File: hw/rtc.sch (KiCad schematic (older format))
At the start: 0 parts

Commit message: hw: add RTC sheet
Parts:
- added BT?: Battery_Cell, symbol Battery_Cell
- added C?: 0.1, symbol C
- added DD?: DS3231, Housings_SOIC:SOIC-16W_7.5x10.3mm_Pitch1.27mm, symbol DS3231
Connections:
- net labels added: +3.3VP, GND, RPI_SCL, RPI_SDA, ~HAT_RST
- wire segments 0 -> 12
- no-connect marks 0 -> 2
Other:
- note added: "NOTE: That chip has integrated reset controller and 50k pull-up R."
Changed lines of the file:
@@
 Comment4 ""
 $EndDescr
+$Comp
+L DS3231 DD?
+U 1 1 5AB3B4DF
+P 4400 5000
+F 0 "DD?" H 4000 5450 60  0000 C CNN
+F 1 "DS3231" H 4400 4550 60  0000 C CNN
+F 2 "Housings_SOIC:SOIC-16W_7.5x10.3mm_Pitch1.27mm" H 4400 5050 60  0001 C CNN
+F 3 "" H 4400 5050 60  0001 C CNN
+	1    4400 5000
+	1    0    0    -1
+$EndComp
+$Comp
+L GND #PWR?
+U 1 1 5AB3BD10
+P 5350 5650
+F 0 "#PWR?" H 5350 5400 50  0001 C CNN
+F 1 "GND" H 5350 5500 50  0000 C CNN
+F 2 "" H 5350 5650 50  0001 C CNN
+F 3 "" H 5350 5650 50  0001 C CNN
+	1    5350 5650
+	1    0    0    -1
+$EndComp
+$Comp
+L +3.3VP #PWR?
+U 1 1 5AB3BD26
+P 5350 5100
+F 0 "#PWR?" H 5500 5050 50  0001 C CNN
+F 1 "+3.3VP" H 5350 5200 50  0000 C CNN
+F 2 "" H 5350 5100 50  0001 C CNN
+F 3 "" H 5350 5100 50  0001 C CNN
+	1    5350 5100
+	1    0    0    -1
+$EndComp
+Text GLabel 3200 4750 0    60   Output ~ 0
+~HAT_RST
+Wire Wire Line
+	3200 4750 3700 4750
+Text GLabel 3200 5250 0    60   Input ~ 0
+RPI_SCL
+Text GLabel 3200 5150 0    60   BiDi ~ 0
+RPI_SDA
+Wire Wire Line
+	3200 5150 3700 5150
+Wire Wire Line
+	3700 5250 3200 5250
+NoConn ~ 3700 5050
+NoConn ~ 5100 4750
+$Comp
+L C C?
+U 1 1 5AB3BFC6
+P 5350 5400
+F 0 "C?" H 5375 5500 50  0000 L CNN
+F 1 "0.1" H 5375 5300 50  0000 L CNN
+F 2 "" H 5388 5250 50  0001 C CNN
+F 3 "" H 5350 5400 50  0001 C CNN
+	1    5350 5400
+	1    0    0    -1
+$EndComp
+Wire Wire Line
+	5350 5100 5350 5250
+Wire Wire Line
+	5350 5550 5350 5650
+Wire Wire Line
+	5100 5250 5200 5250
+Wire Wire Line
+	5200 5250 5200 5600
+Wire Wire Line
+	5200 5600 5650 5600
+Connection ~ 5350 5600
+Wire Wire Line
+	5100 5150 5350 5150
+Connection ~ 5350 5150
+$Comp
+L Battery_Cell BT?
+U 1 1 5AB3C398
+P 5650 5250
+F 0 "BT?" H 5750 5350 50  0000 L CNN
+F 1 "Battery_Cell" H 5750 5250 50  0000 L CNN
+F 2 "" V 5650 5310 50  0001 C CNN
+F 3 "" V 5650 5310 50  0001 C CNN
+	1    5650 5250
+	1    0    0    -1
+$EndComp
+Wire Wire Line
+	5100 4950 5650 4950
+Wire Wire Line
+	5650 4950 5650 5050
+Wire Wire Line
+	5650 5600 5650 5350
+Text Notes 2850 6200 0    60   ~ 0
+NOTE: That chip has integrated reset controller and 50k pull-up R.
 $EndSCHEMATC

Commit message: switch to KiCAD 5 (nightly)
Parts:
- removed BT?: Battery_Cell, symbol Battery_Cell
- removed C?: 0.1, symbol C
- added BT?: Battery_Cell, symbol Device:Battery_Cell
- added C?: 0.1, symbol Device:C
- DD?: symbol DS3231 -> ic:DS3231
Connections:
- wire segments 12 -> 15
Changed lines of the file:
@@
-EESchema Schematic File Version 2
-LIBS:power
-LIBS:device
-LIBS:transistors
-LIBS:conn
-LIBS:linear
-LIBS:regul
-LIBS:74xx
-LIBS:cmos4000
-LIBS:adc-dac
-LIBS:memory
-LIBS:xilinx
-LIBS:microcontrollers
-LIBS:dsp
-LIBS:microchip
-LIBS:analog_switches
-LIBS:motorola
-LIBS:texas
-LIBS:intel
-LIBS:audio
-LIBS:interface
-LIBS:digital-audio
-LIBS:philips
-LIBS:display
-LIBS:cypress
-LIBS:siliconi
-LIBS:opto
-LIBS:atmel
-LIBS:contrib
-LIBS:valves
-LIBS:rpi_con
-LIBS:ic
-LIBS:dronecode_con
+EESchema Schematic File Version 4
 LIBS:obc-drone-hat-cache
-EELAYER 25 0
+EELAYER 26 0
 EELAYER END
 $Descr A4 8268 11693 portrait
@@
 $EndDescr
 $Comp
-L DS3231 DD?
+L ic:DS3231 DD?
 U 1 1 5AB3B4DF
 P 4400 5000
@@
 $EndComp
 $Comp
-L GND #PWR?
+L power:GND #PWR?
 U 1 1 5AB3BD10
 P 5350 5650
@@
 $EndComp
 $Comp
-L +3.3VP #PWR?
+L power:+3.3VP #PWR?
 U 1 1 5AB3BD26
 P 5350 5100
@@
 NoConn ~ 3700 5050
 NoConn ~ 5100 4750
-$Comp
-L C C?
-U 1 1 5AB3BFC6
-P 5350 5400
-F 0 "C?" H 5375 5500 50  0000 L CNN
-F 1 "0.1" H 5375 5300 50  0000 L CNN
-F 2 "" H 5388 5250 50  0001 C CNN
-F 3 "" H 5350 5400 50  0001 C CNN
-	1    5350 5400
-	1    0    0    -1
-$EndComp
 Wire Wire Line
-	5350 5100 5350 5250
+	5350 5100 5350 5150
 Wire Wire Line
-	5350 5550 5350 5650
+	5350 5550 5350 5600
 Wire Wire Line
 	5100 5250 5200 5250
@@
 	5200 5250 5200 5600
 Wire Wire Line
-	5200 5600 5650 5600
+	5200 5600 5350 5600
 Connection ~ 5350 5600
 Wire Wire Line
 	5100 5150 5350 5150
 Connection ~ 5350 5150
-$Comp
-L Battery_Cell BT?
-U 1 1 5AB3C398
-P 5650 5250
-F 0 "BT?" H 5750 5350 50  0000 L CNN
-F 1 "Battery_Cell" H 5750 5250 50  0000 L CNN
-F 2 "" V 5650 5310 50  0001 C CNN
-F 3 "" V 5650 5310 50  0001 C CNN
-	1    5650 5250
-	1    0    0    -1
-$EndComp
 Wire Wire Line
 	5100 4950 5650 4950
@@
 Text Notes 2850 6200 0    60   ~ 0
 NOTE: That chip has integrated reset controller and 50k pull-up R.
+Wire Wire Line
+	5350 5600 5350 5650
+Wire Wire Line
+	5350 5600 5650 5600
+Wire Wire Line
+	5350 5150 5350 5250
+$Comp
+L Device:Battery_Cell BT?
+U 1 1 5AC0D5A2
+P 5650 5250
+F 0 "BT?" H 5768 5346 50  0000 L CNN
+F 1 "Battery_Cell" H 5768 5255 50  0000 L CNN
+F 2 "" V 5650 5310 50  0001 C CNN
+F 3 "~" V 5650 5310 50  0001 C CNN
+	1    5650 5250
+	1    0    0    -1
+$EndComp
+$Comp
+L Device:C C?
+U 1 1 5AC0D763
+P 5350 5400
+F 0 "C?" H 5465 5446 50  0000 L CNN
+F 1 "0.1" H 5465 5355 50  0000 L CNN
+F 2 "" H 5388 5250 50  0001 C CNN
+F 3 "~" H 5350 5400 50  0001 C CNN
+	1    5350 5400
+	1    0    0    -1
+$EndComp
 $EndSCHEMATC

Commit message: hw: start stm page
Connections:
- net +3.3VP renamed +3V3
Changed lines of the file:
@@
-	1    0    0    -1
-$EndComp
-$Comp
-L power:+3.3VP #PWR?
-U 1 1 5AB3BD26
-P 5350 5100
-F 0 "#PWR?" H 5500 5050 50  0001 C CNN
-F 1 "+3.3VP" H 5350 5200 50  0000 C CNN
-F 2 "" H 5350 5100 50  0001 C CNN
-F 3 "" H 5350 5100 50  0001 C CNN
-	1    5350 5100
 	1    0    0    -1
 $EndComp
@@
 	1    0    0    -1
 $EndComp
+$Comp
+L power:+3.3V #PWR?
+U 1 1 5AC432E2
+P 5350 5100
+F 0 "#PWR?" H 5350 4950 50  0001 C CNN
+F 1 "+3.3V" H 5500 5200 50  0000 C CNN
+F 2 "" H 5350 5100 50  0001 C CNN
+F 3 "" H 5350 5100 50  0001 C CNN
+	1    5350 5100
+	1    0    0    -1
+$EndComp

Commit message: hw: update libs
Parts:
- DD?: symbol ic:DS3231 -> hat-ic:DS3231
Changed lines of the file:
@@
 $EndDescr
 $Comp
-L ic:DS3231 DD?
+L hat-ic:DS3231 DD?
 U 1 1 5AB3B4DF
 P 4400 5000

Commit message: hw: sch ready
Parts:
- gave numbers to parts that had none: 3
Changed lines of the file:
@@
 $EndDescr
 $Comp
-L hat-ic:DS3231 DD?
+L hat-ic:DS3231 DD5
 U 1 1 5AB3B4DF
 P 4400 5000
-F 0 "DD?" H 4000 5450 60  0000 C CNN
+F 0 "DD5" H 4000 5450 60  0000 C CNN
 F 1 "DS3231" H 4400 4550 60  0000 C CNN
 F 2 "Housings_SOIC:SOIC-16W_7.5x10.3mm_Pitch1.27mm" H 4400 5050 60  0001 C CNN
@@
 $EndComp
 $Comp
-L power:GND #PWR?
+L power:GND #PWR048
 U 1 1 5AB3BD10
 P 5350 5650
-F 0 "#PWR?" H 5350 5400 50  0001 C CNN
+F 0 "#PWR048" H 5350 5400 50  0001 C CNN
 F 1 "GND" H 5350 5500 50  0000 C CNN
 F 2 "" H 5350 5650 50  0001 C CNN
@@
 	5350 5150 5350 5250
 $Comp
-L Device:Battery_Cell BT?
+L Device:Battery_Cell BT1
 U 1 1 5AC0D5A2
 P 5650 5250
-F 0 "BT?" H 5768 5346 50  0000 L CNN
+F 0 "BT1" H 5768 5346 50  0000 L CNN
 F 1 "Battery_Cell" H 5768 5255 50  0000 L CNN
 F 2 "" V 5650 5310 50  0001 C CNN
@@
 $EndComp
 $Comp
-L Device:C C?
+L Device:C C12
 U 1 1 5AC0D763
 P 5350 5400
-F 0 "C?" H 5465 5446 50  0000 L CNN
+F 0 "C12" H 5465 5446 50  0000 L CNN
 F 1 "0.1" H 5465 5355 50  0000 L CNN
 F 2 "" H 5388 5250 50  0001 C CNN
@@
 $EndComp
 $Comp
-L power:+3.3V #PWR?
+L power:+3.3V #PWR047
 U 1 1 5AC432E2
 P 5350 5100
-F 0 "#PWR?" H 5350 4950 50  0001 C CNN
+F 0 "#PWR047" H 5350 4950 50  0001 C CNN
 F 1 "+3.3V" H 5500 5200 50  0000 C CNN
 F 2 "" H 5350 5100 50  0001 C CNN

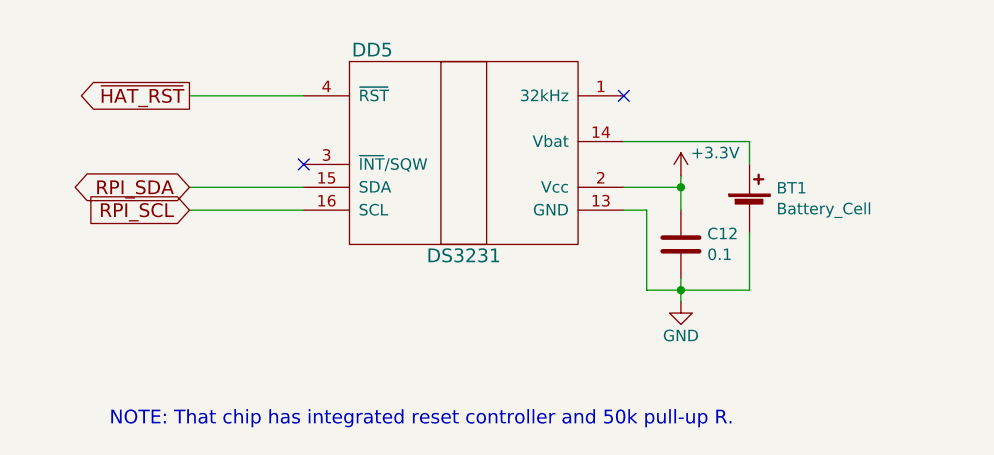
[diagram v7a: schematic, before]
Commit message: hw: fix ERC
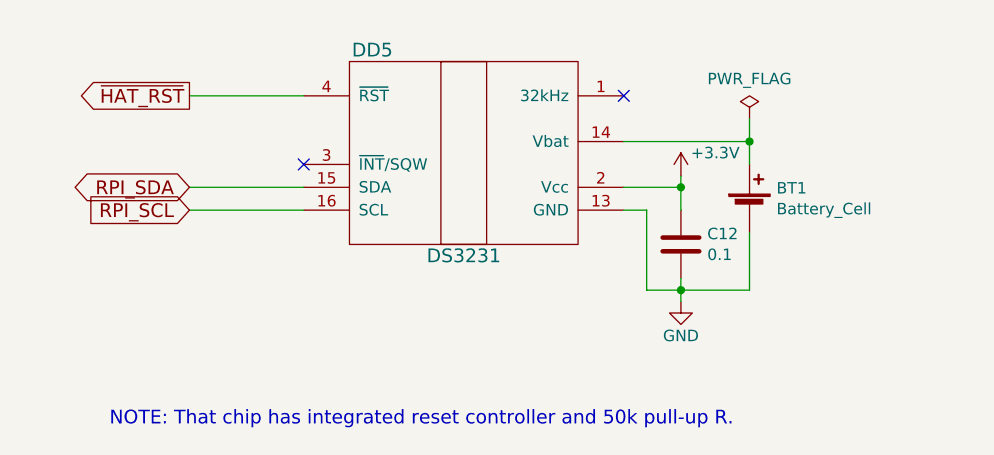
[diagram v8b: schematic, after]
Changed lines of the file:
@@
 	1    0    0    -1
 $EndComp
+$Comp
+L power:PWR_FLAG #FLG0103
+U 1 1 5AE576E6
+P 5650 4850
+F 0 "#FLG0103" H 5650 4925 50  0001 C CNN
+F 1 "PWR_FLAG" H 5650 5024 50  0000 C CNN
+F 2 "" H 5650 4850 50  0001 C CNN
+F 3 "" H 5650 4850 50  0001 C CNN
+	1    5650 4850
+	1    0    0    -1
+$EndComp
+Wire Wire Line
+	5650 4850 5650 4950
+Connection ~ 5650 4950
 $EndSCHEMATC
